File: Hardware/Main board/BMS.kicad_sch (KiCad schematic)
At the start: 15 parts, among them J3 Conn_01x03, U1 BQ25895RTW

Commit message: Reworking BMS
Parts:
- added NT1: NetTie_2, symbol Device:NetTie_2
- added U11: BQ25895, symbol BQ25895-accurate:BQ25895-accurate
- U1: Design guide (none) -> https://www.ti.com/lit/ug/sluuba2b/sluuba2b.pdf
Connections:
- new net: U11.13 (BAT), U11.14 (BAT)
- new net: U11.15 (SYS), U11.16 (SYS)
- new net AGND: NT1.1
- new net PGND: NT1.2, U11.17 (PGND), U11.18 (PGND), U11.25 (PAD)

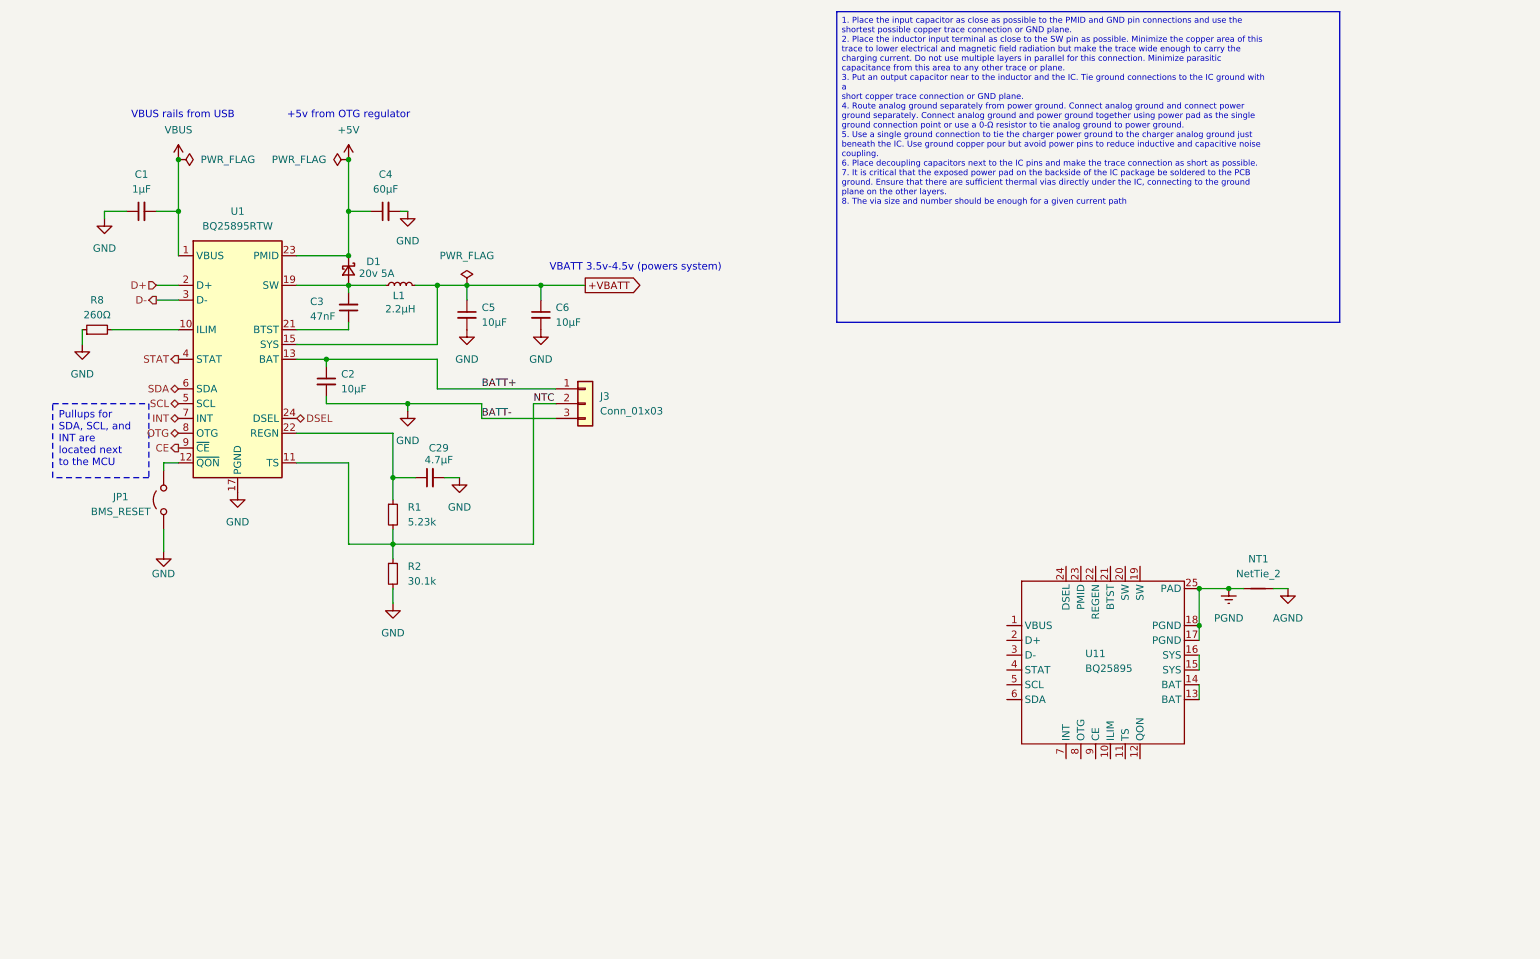
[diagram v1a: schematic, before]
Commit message: refactor BMD schematic
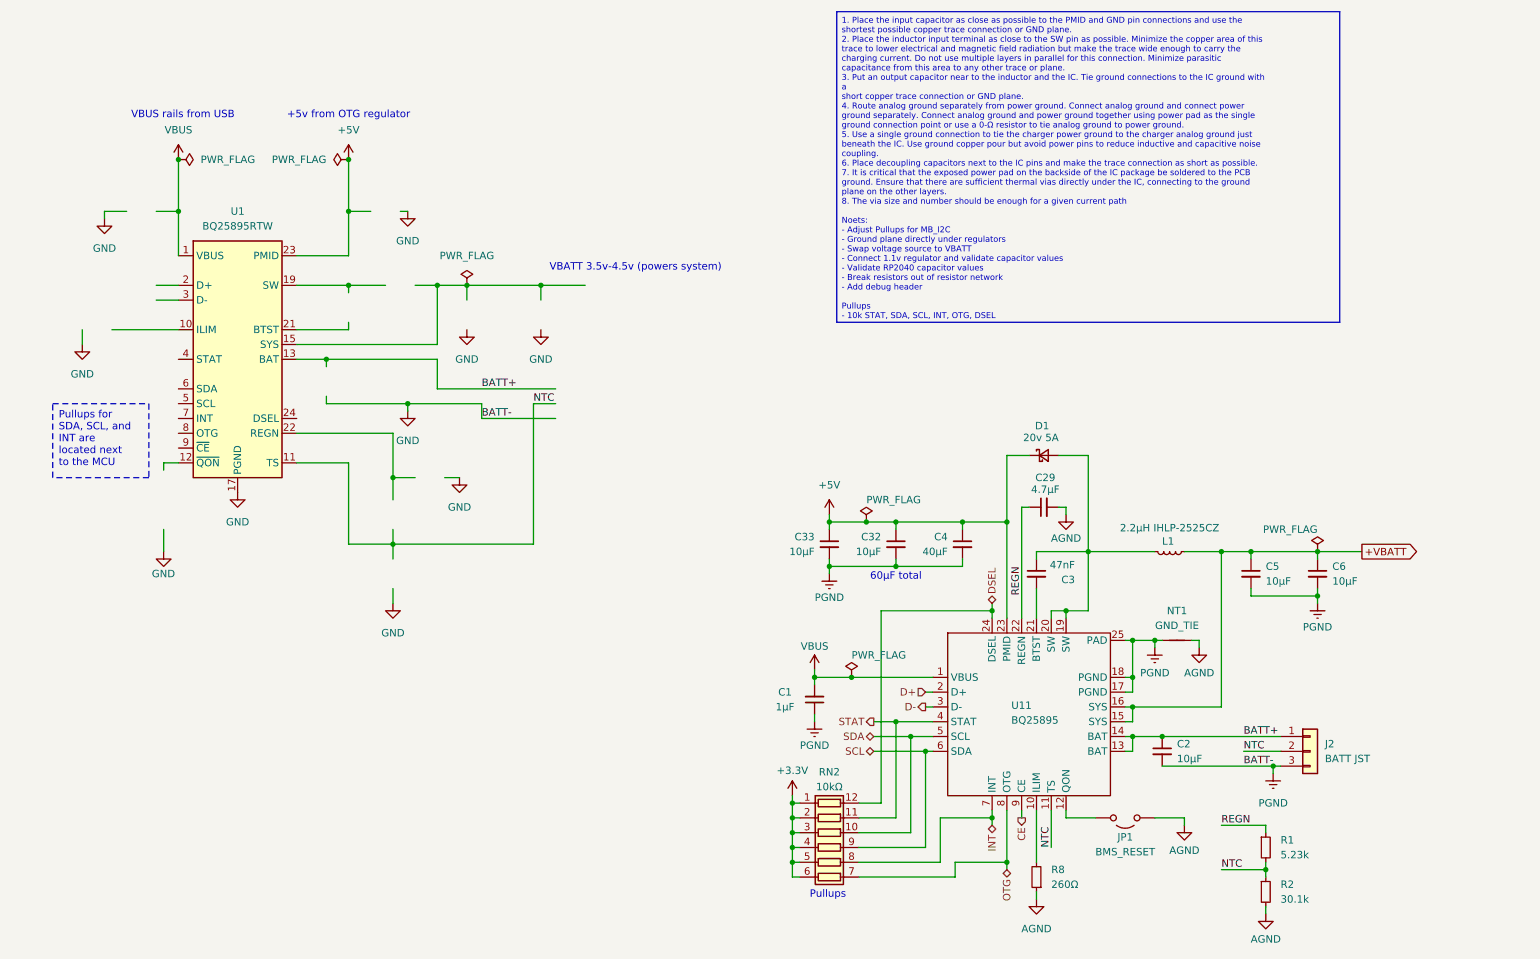
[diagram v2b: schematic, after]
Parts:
- removed J3: Conn_01x03, Connector_JST:JST_XH_S3B-XH-SM4-TB_1x03-1MP_P2.50mm_Horizontal, symbol Connector_Generic:Conn_01x03
- added C32, C33: 10μF, Capacitor_SMD:C_0603_1608Metric, symbol Device:C_Small
- added J2: BATT JST, Connector_JST:JST_XH_S3B-XH-SM4-TB_1x03-1MP_P2.50mm_Horizontal, symbol Connector_Generic:Conn_01x03
- added RN2: 10kΩ, symbol Device:R_Pack06
- C4: value 60μF -> 40μF
- L1: value 2.2µH -> 2.2µH IHLP-2525CZ; footprint Inductor_SMD:L_1210_3225Metric -> Inductor_SMD:L_Vishay_IHLP-2525; LCSC Part # (none) -> C540967
- NT1: value NetTie_2 -> GND_TIE
- U11: footprint (none) -> Package_DFN_QFN:Texas_RTW_WQFN-24-1EP_4x4mm_P0.5mm_EP2.7x2.7mm_ThermalVias; Design guide (none) -> https://www.ti.com/lit/ug/sluuba2b/sluuba2b.pdf
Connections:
- net PGND is gone; now on net GND: NT1.2, U11.17 (PGND), U11.18 (PGND), U11.25 (PAD)
- net +5V: now also U11.23 (PMID), C32.1, C33.1
- net +VBATT: now also U11.15 (SYS), U11.16 (SYS); no longer U1.15 (SYS), U1.16 (SYS)
- net AGND: now also C29.2, JP1.1 (A), R2.2, R8.1
- net BATT+: now also U11.13 (BAT), U11.14 (BAT), J2.1 (Pin_1)
- net CE: now also U11.9 (CE); no longer U1.9 (~{CE})
- net D+: now also U11.2 (D+); no longer U1.2 (D+)
- net D-: now also U11.3 (D-); no longer U1.3 (D-)
- net DSEL: now also U11.24 (DSEL), RN2.12 (R1.2); no longer U1.24 (DSEL)
- net GND: now also C32.2, C33.2, J2.3 (Pin_3); no longer C29.2, JP1.1 (A), R2.2, R8.1
- net INT: now also U11.7 (INT), RN2.8 (R5.2); no longer U1.7 (INT)
- net NTC: now also U11.11 (TS), J2.2 (Pin_2)
- net OTG: now also U11.8 (OTG), RN2.7 (R6.2); no longer U1.8 (OTG)
- net SCL: now also U11.6 (SDA), RN2.9 (R4.2); no longer U1.5 (SCL)
- net SDA: now also U11.5 (SCL), RN2.10 (R3.2); no longer U1.6 (SDA)
- net STAT: now also U11.4 (STAT), RN2.11 (R2.2); no longer U1.4 (STAT)
- net VBUS: now also U11.1 (VBUS)
- net at JP1.2 (B): now also U11.12 (QON); no longer U1.12 (~{QON})
- net REGN: now reaches C29.1, R1.1
- net REGN: now also U11.22 (REGN); no longer U1.22 (REGN)
- net at R8.2: now also U11.10 (ILIM); no longer U1.10 (ILIM)
- net at C3.1: now also D1.2 (A), L1.1, U11.19 (SW), U11.20 (SW); no longer U1.21 (BTST)
- net at U11.21 (BTST): now also C3.2
- new net: U1.15 (SYS), U1.16 (SYS)
- new net: U1.19 (SW), U1.20 (SW)
- new net +3.3V: RN2.1 (R1.1), RN2.2 (R2.1), RN2.3 (R3.1), RN2.4 (R4.1), RN2.5 (R5.1), RN2.6 (R6.1)
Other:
- note added: "60μF total"
- note added: "Pullups"
- moved on the sheet: C1, NT1, U11

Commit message: complete BMS layout
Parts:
- L1: value 2.2µH IHLP-2525CZ -> 2.2µH; JLCPCB Parts URL (none) -> https://jlcpcb.com/partdetail/VishayIntertech-IHLP2525CZER2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
- R1: value 5.23k -> 5.23kΩ
- R2: value 30.1k -> 30.1kΩ
- RN2: value 10kΩ -> 6x 10kΩ
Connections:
- net +VBATT: now also L1.1; no longer L1.2
- net SCL: now also RN2.10 (R3.2), U11.5 (SCL); no longer RN2.9 (R4.2), U11.6 (SDA)
- net SDA: now also RN2.9 (R4.2), U11.6 (SDA); no longer RN2.10 (R3.2), U11.5 (SCL)
- net at C3.1, D1.2 (A), U11.19 (SW)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: now also L1.2; no longer L1.1
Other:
- note added: "3-pin battery JST"
- note added: "5A ILimit"
- note added: "VBATT 3.5v-4.5v"
- note removed: "VBATT 3.5v-4.5v (powers system)"
- moved on the sheet: C1, C2, C29, C3, C32, C33, C4, C5, C6, D1, J2, JP1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

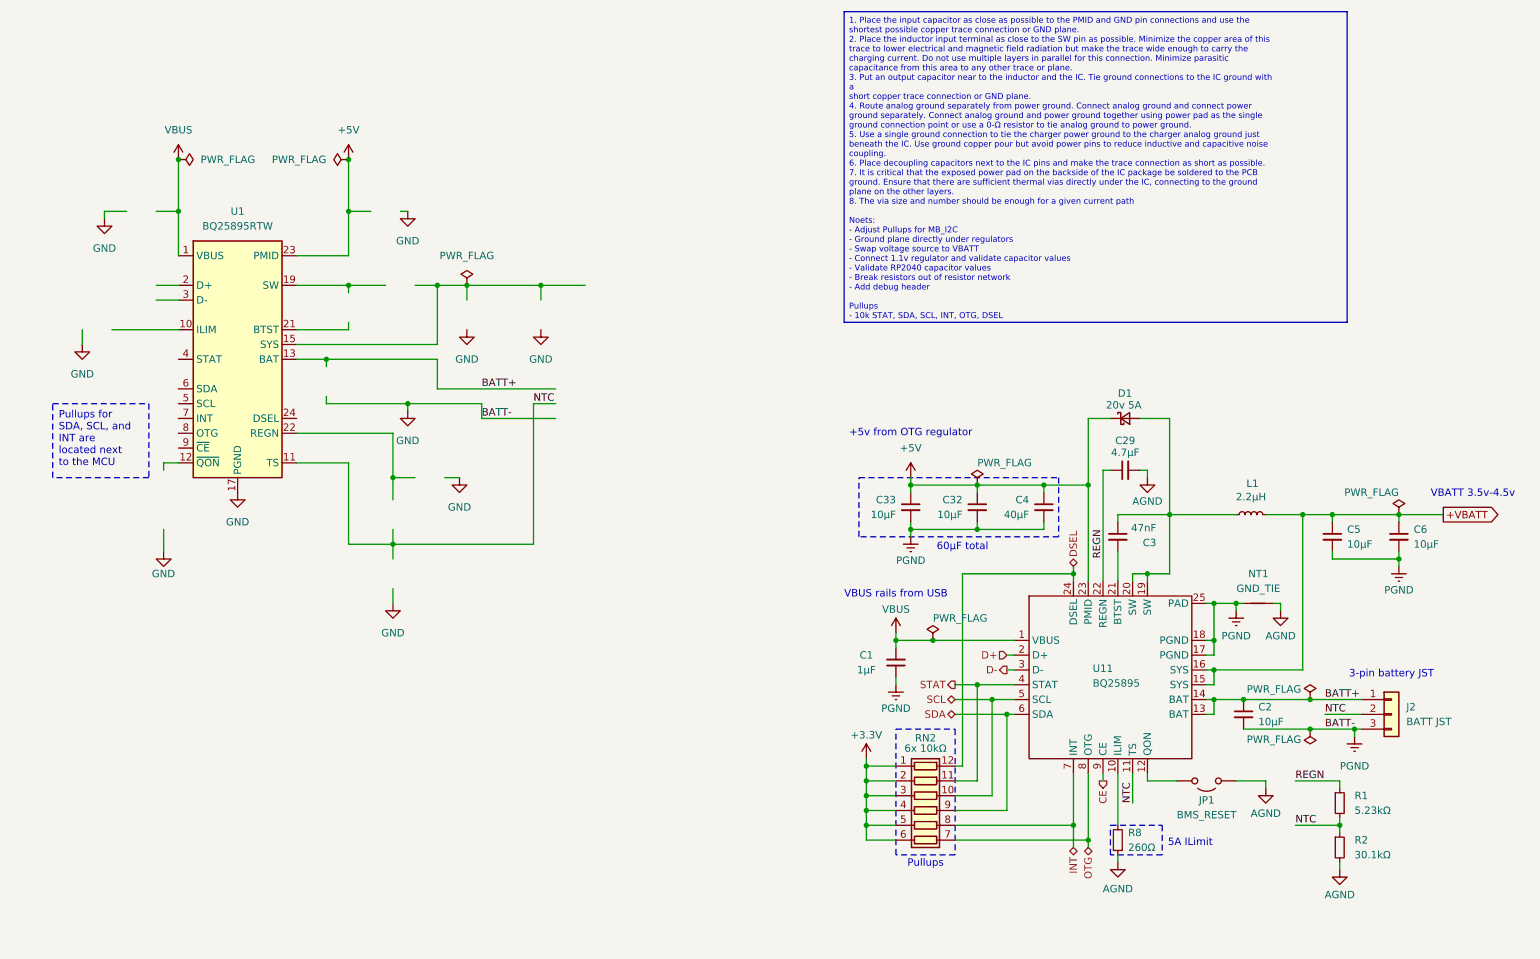
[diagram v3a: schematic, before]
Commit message: refactor PCB for new BMS layout
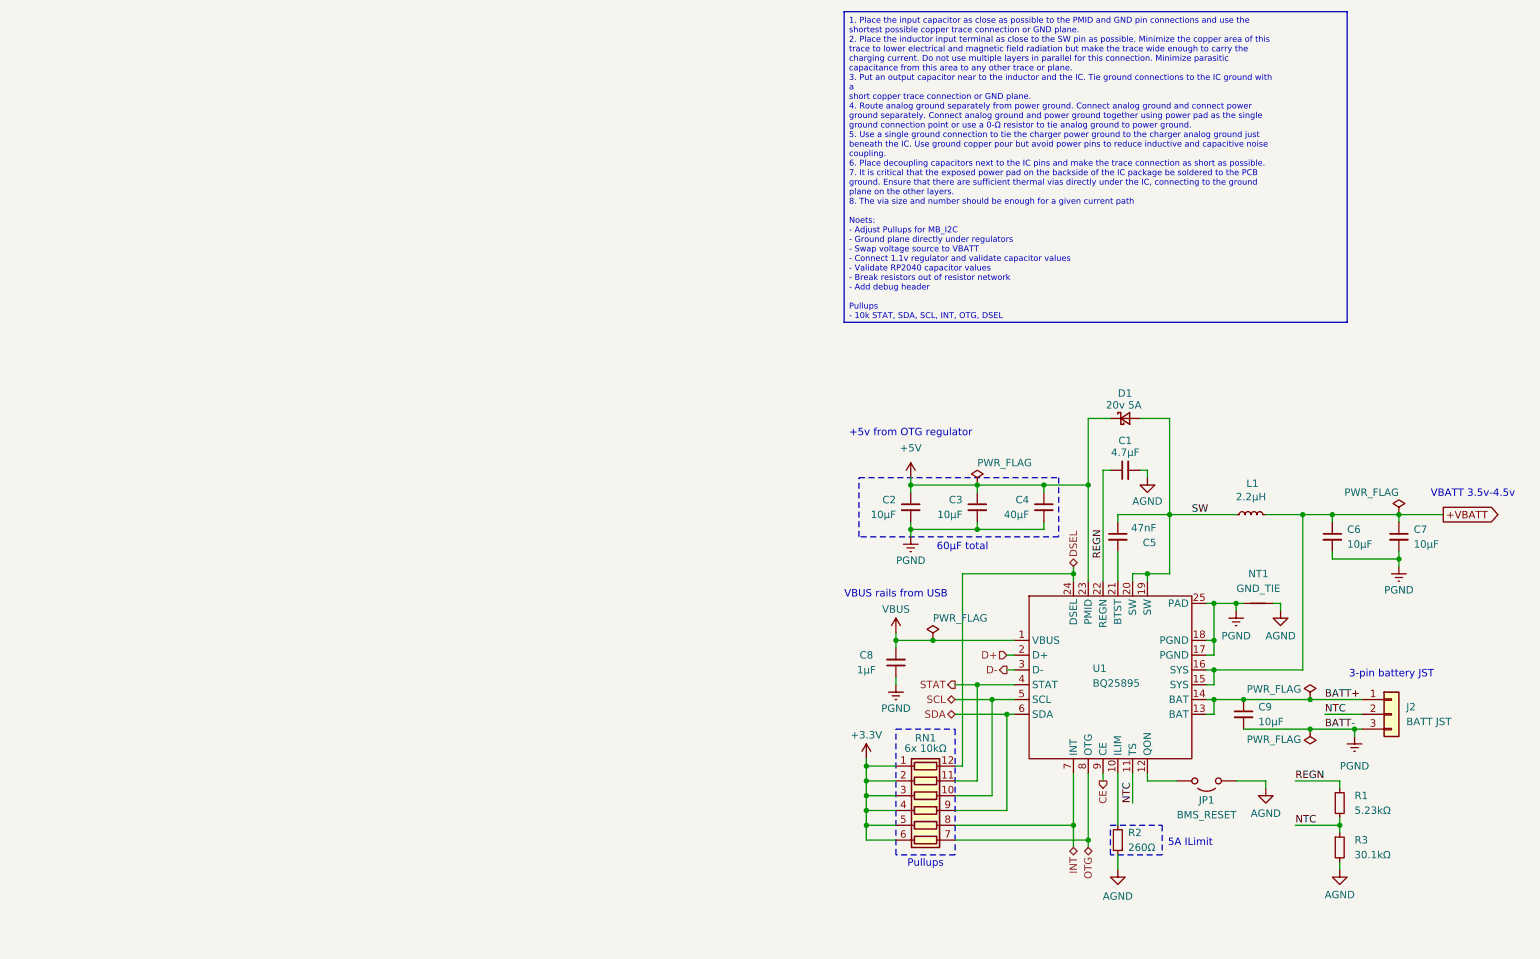
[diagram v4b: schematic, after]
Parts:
- removed U1: BQ25895RTW, Package_DFN_QFN:Texas_RTW_WQFN-24-1EP_4x4mm_P0.5mm_EP2.7x2.7mm_ThermalVias, symbol Battery_Management:BQ25895RTW
- NT1: footprint (none) -> NetTie:NetTie-2_SMD_Pad2.0mm
- R2: renamed from R8; footprint Resistor_SMD:R_0805_2012Metric -> Resistor_SMD:R_0402_1005Metric
- renumbered C29 to C1, C33 to C2, C32 to C3, C3 to C5, C5 to C6, C6 to C7, C1 to C8, C2 to C9, R2 to R3, RN2 to RN1, U11 to U1
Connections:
- net SW: now reaches C5.1, D1.2 (A), L1.2, U1.19 (SW), U1.20 (SW)
- net GND renamed PGND

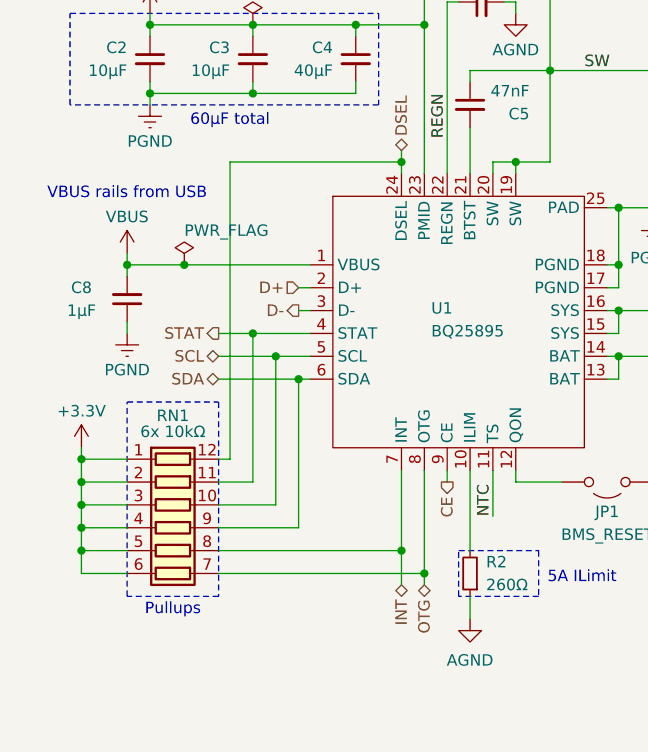
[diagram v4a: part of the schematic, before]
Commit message: All components routed
- broke out resistor network into individual resistors
- AGND tied to PGND by BMS
- repositioned GPIO positions
- length-matched USB to within 0.1mm
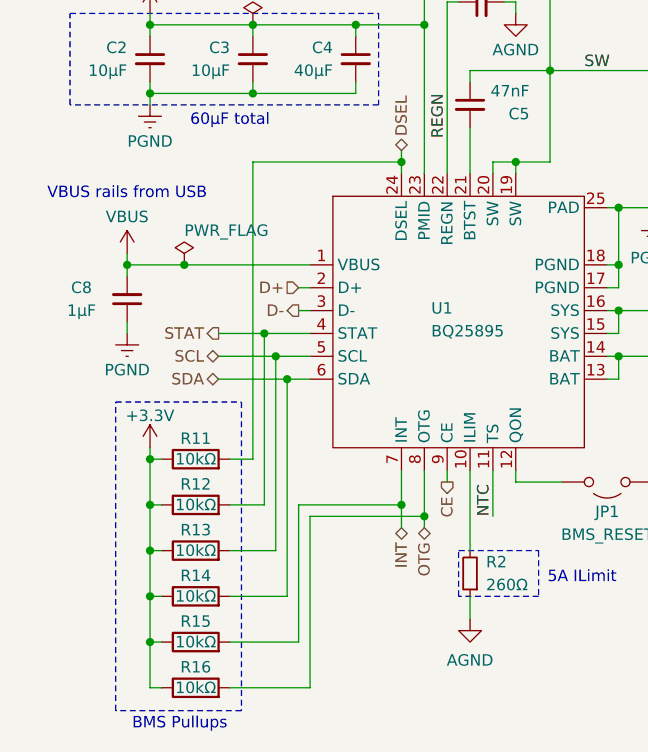
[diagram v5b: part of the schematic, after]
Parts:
- removed RN1: 6x 10kΩ, symbol Device:R_Pack06
- added R11, R12, R13, R14, R15, R16: 10kΩ, Resistor_SMD:R_0603_1608Metric, symbol Device:R
- NT1: footprint NetTie:NetTie-2_SMD_Pad2.0mm -> NetTie:NetTie-2_SMD_Pad0.5mm
- R2: footprint Resistor_SMD:R_0402_1005Metric -> Resistor_SMD:R_0603_1608Metric
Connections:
- net +3.3V: now also R11.1, R12.1, R13.1, R14.1, R15.1, R16.1
- net DSEL: now also R11.2
- net INT: now also R15.2
- net OTG: now also R16.2
- net SCL: now also R13.2
- net SDA: now also R14.2
- net STAT: now also R12.2
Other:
- note added: "BMS Pullups"
- note removed: "Pullups"
